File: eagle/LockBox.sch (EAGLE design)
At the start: 19 parts

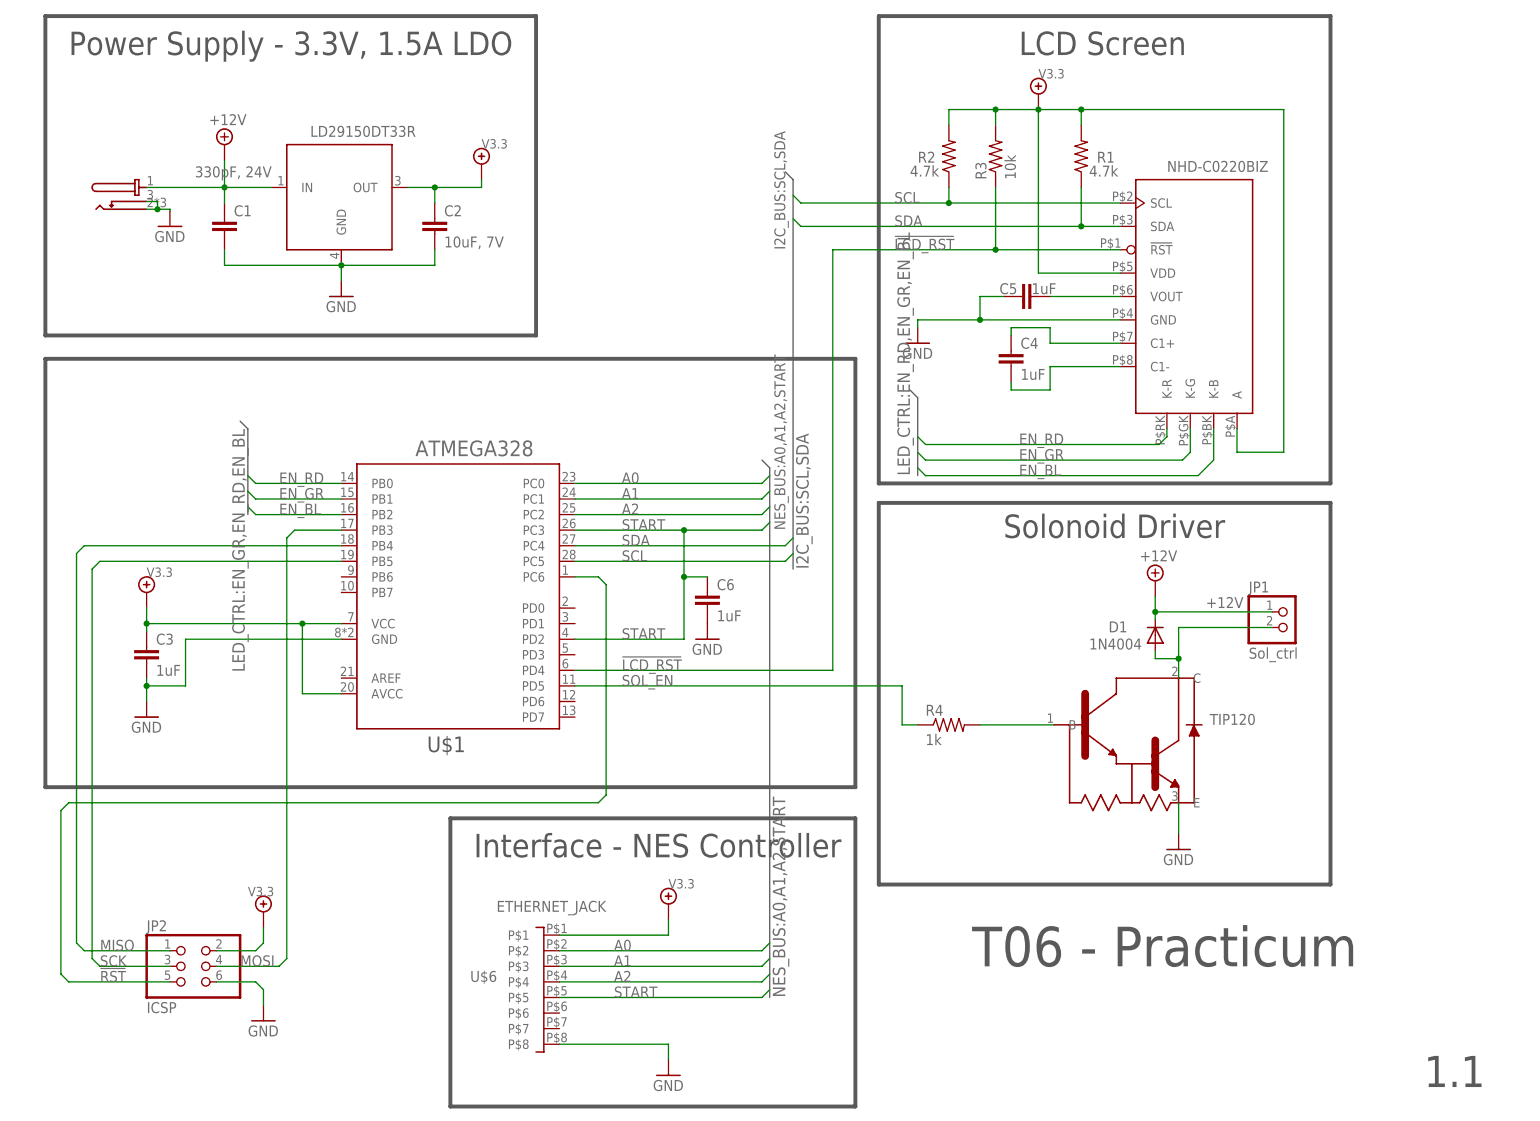
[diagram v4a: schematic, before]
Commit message: Removed the LCD screen from the .sch and inserted a pin header in its place.
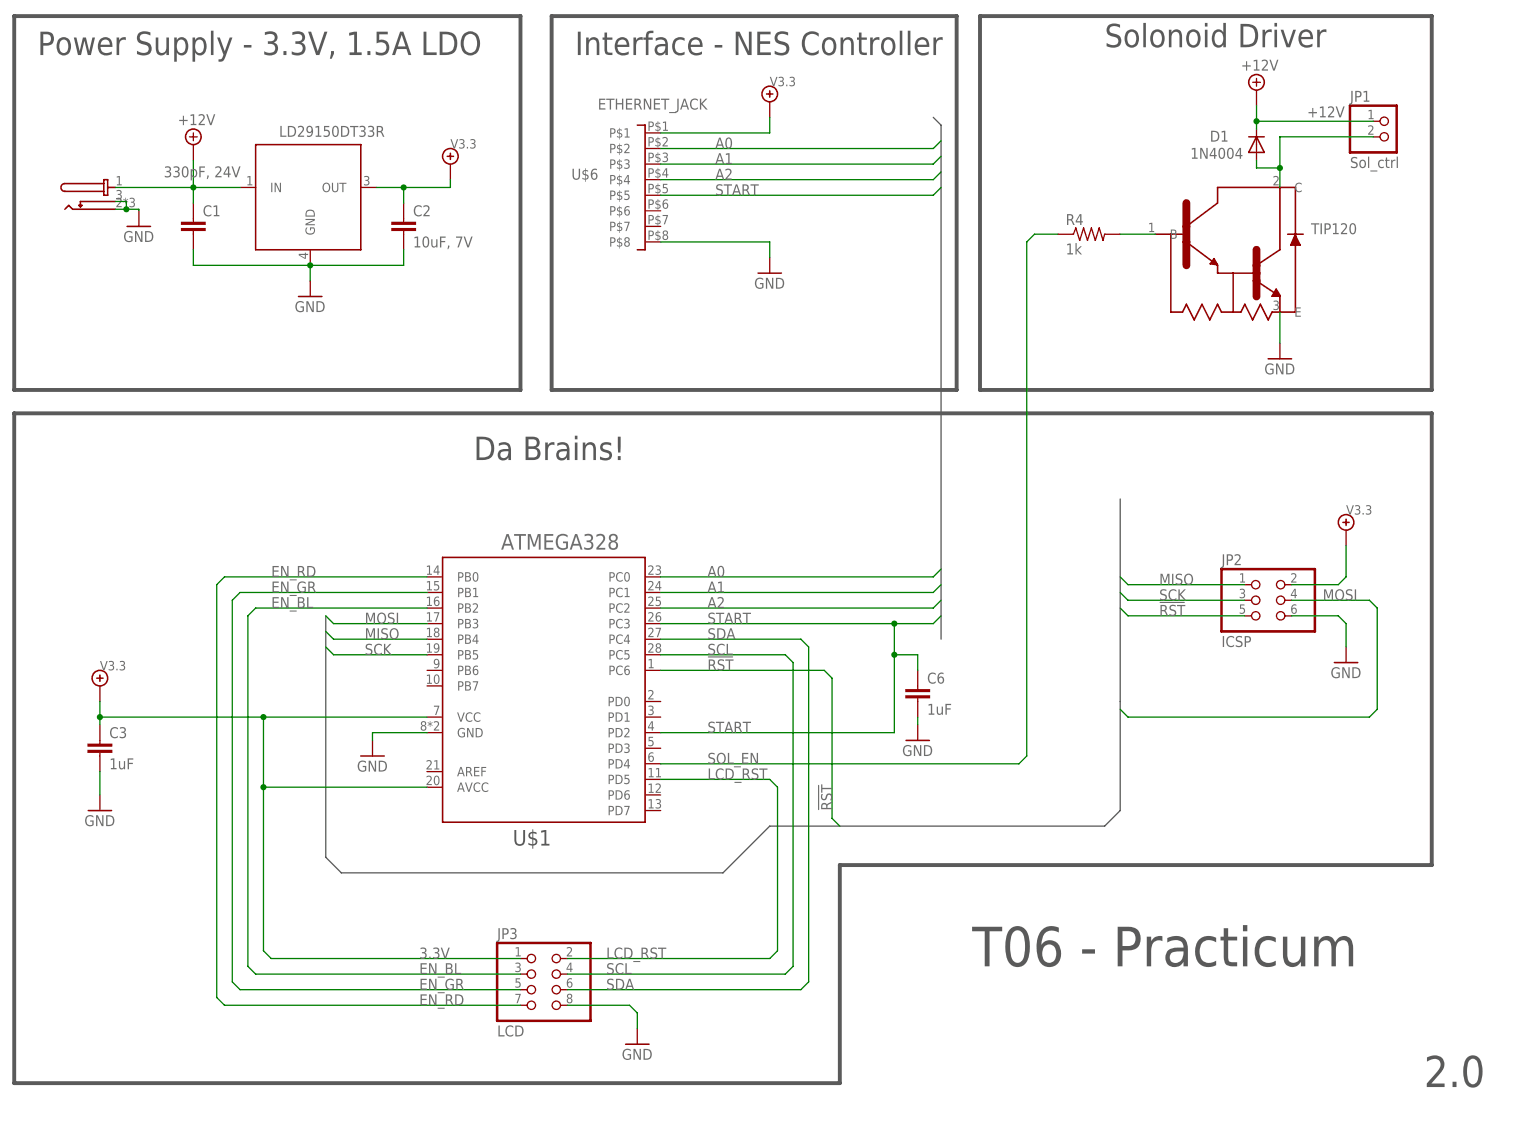
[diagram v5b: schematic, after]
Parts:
- removed C4, C5: 1uF, LockBox:C
- removed R1, R2: 4.7k, LockBox:R-US_M0805
- removed R3: 10k, LockBox:R-US_M0805
- removed U$5: NHD-C0220BIZ, LockBox:NHD-C0220BIZ
- added JP3: LCD, LockBox:PINHD-2X4
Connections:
- removed net !LCD_RST: R3.1, U$1.PD4, U$5.!RST
- removed net N$2: C4.1, U$5.C1+
- removed net N$3: C4.2, U$5.C1-
- removed net N$4: C5.2, U$5.VOUT
- new net LCD_RST: JP3.2, U$1.PD5
- new net P$1: JP2.2
- net 3.3V: now also JP3.1; no longer JP2.2, R1.2, R2.2, R3.2, U$5.A, U$5.VDD
- net EN_BL: now also JP3.3; no longer U$5.K-B
- net EN_GR: now also JP3.5; no longer U$5.K-G
- net EN_RD: now also JP3.7; no longer U$5.K-R
- net GND: now also JP3.8; no longer C5.1, U$5.GND
- net SCL: now also JP3.4; no longer R2.1, U$5.SCL
- net SDA: now also JP3.6; no longer R1.1, U$5.SDA
- net SOL_EN: now also U$1.PD4; no longer U$1.PD5
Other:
- note added: "2.0"
- note added: "Da Brains!"
- note removed: "1.1"
- note removed: "LCD Screen"
- moved on the sheet: C1, C2, C3, C6, D1, JP1, JP2, R4, U$1, U$6

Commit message: Added transister pulldown network for LCD-LED backlighting
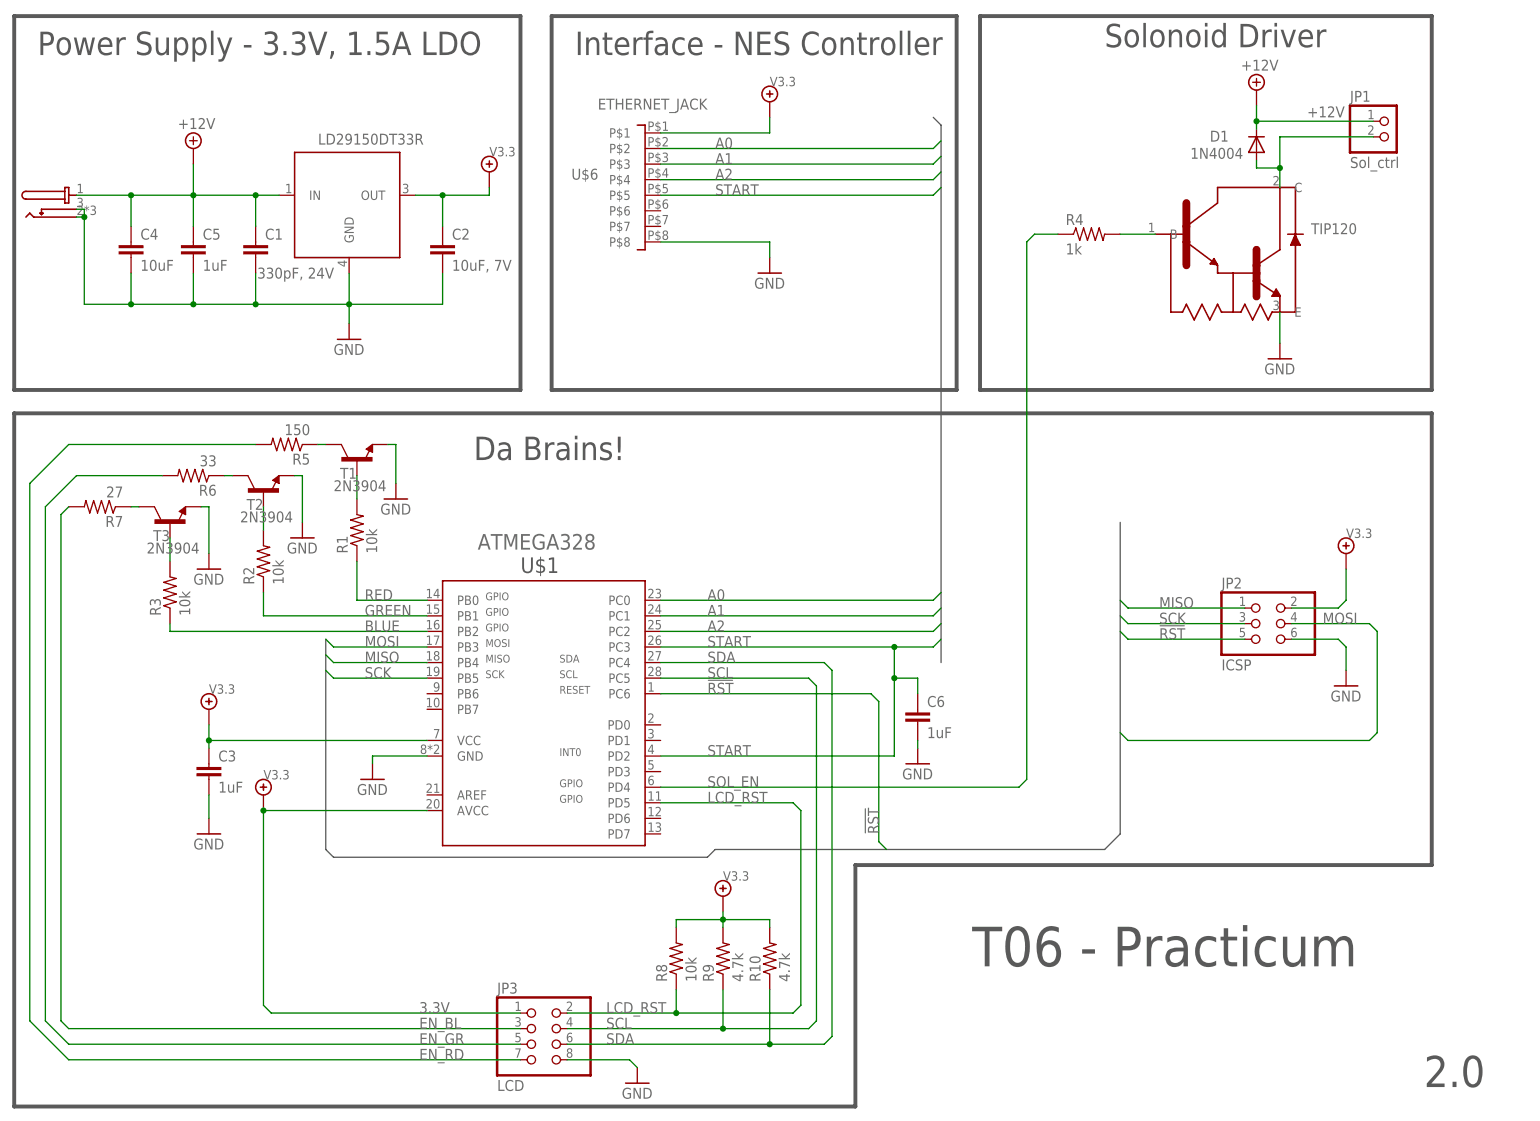
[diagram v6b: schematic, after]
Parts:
- added C4: 10uF, LockBox:C
- added C5: 1uF, LockBox:C
- added R1, R2, R3, R8: 10k, LockBox:R-US_R0805
- added R10, R9: 4.7k, LockBox:R-US_R0805
- added R5: 150, LockBox:R-US_R0805
- added R6: 33, LockBox:R-US_R0805
- added R7: 27, LockBox:R-US_R0805
- added T1, T2, T3: 2N3904, LockBox:2N3904
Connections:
- removed net P$1: JP2.2
- new net BLUE: R3.1, U$1.PB2
- new net GREEN: R2.1, U$1.PB1
- new net N$10: R7.1, T3.C
- new net N$11: R6.1, T2.C
- new net N$12: R5.1, T1.C
- new net N$6: R1.2, T1.B
- new net N$7: R2.2, T2.B
- new net N$8: R3.2, T3.B
- new net RED: R1.1, U$1.PB0
- net +12V: now also C4.1, C5.1
- net 3.3V: now also JP2.2, R10.2, R8.2, R9.2
- net EN_BL: now also R7.2; no longer U$1.PB2
- net EN_GR: now also R6.2; no longer U$1.PB1
- net EN_RD: now also R5.2; no longer U$1.PB0
- net GND: now also C4.2, C5.2, T1.E, T2.E, T3.E
- net LCD_RST: now also R8.1
- net SCL: now also R9.1
- net SDA: now also R10.1
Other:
- moved on the sheet: C1, C2, C3, C6, JP2, JP3, U$1
